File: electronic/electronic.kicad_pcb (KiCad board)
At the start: 2 copper layers, 19 parts, among them J1 M_BAT01, J10 BMP01, J11 MPU6050_01, J12 NEO_06_01, J14 OLED, J15 HCSR01, J16 HCSR01, J17 HCSR01, J18 HCSR01, J2 M_SIG01, J3 M_SIG01, J4 M_BAT01, J5 M_SIG01, J6 M_BAT01, J7 M_SIG01, J8 M_BAT01, J9 DHT01, U10 DEVKIT_V1_ESP32-WROOM-32

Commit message: chore: PCB design added to the project
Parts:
- added C17: 220u, Capacitor_THT:C_Radial_D8.0mm_H11.5mm_P3.50mm, F.Cu at (104.5, 52.5)
- added J19: BAT, custom:DG301-5.0-2P-1X, F.Cu at (98.0, 67.0)
- added U14: L7805, Package_TO_SOT_SMD:TO-252-2, F.Cu at (97.2, 50.5)
- J16: value HCSR01 -> HCSR02
- J17: value HCSR01 -> HCSR03
- J18: value HCSR01 -> HCSR04
- J3: value M_SIG01 -> M_SIG02
- J4: value M_BAT01 -> M_BAT02
- J5: value M_SIG01 -> M_SIG03
- J6: value M_BAT01 -> M_BAT03
- J7: value M_SIG01 -> M_SIG04
- J8: value M_BAT01 -> M_BAT04
- J9: footprint Connector_PinHeader_2.54mm:PinHeader_1x04_P2.54mm_Vertical -> custom:DHT22
- moved J16 125.8 mm to (17.5, 39.9)
- moved J6 113.0 mm to (21.0, 68.5), turned to 180 degrees
- moved J5 102.7 mm to (21.0, 61.5), turned to 180 degrees
- moved J12 90.7 mm to (64.9, 58.5), turned to 90 degrees
- moved J15 90.2 mm to (69.5, 18.0), turned to -90 degrees
- moved J2 88.4 mm to (18.5, 25.5)
- moved J14 81.7 mm to (94.9, 32.0), turned to 90 degrees
- moved J11 81.5 mm to (60.0, 30.8)
- moved J17 79.5 mm to (61.9, 68.5), turned to 90 degrees
- moved J1 78.3 mm to (21.0, 19.5), turned to 180 degrees
- moved R1 64.7 mm to (76.0, 43.7)
- moved J10 60.1 mm to (88.3, 25.0), turned to 90 degrees
- moved U10 54.0 mm to (39.8, 46.1)
- moved J4 51.3 mm to (112.5, 19.5), turned to 180 degrees
- moved J18 48.9 mm to (113.5, 46.5), turned to 180 degrees
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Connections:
- U10 pad 11: MOTOR04 -> MOTOR01
- U10 pad 12: MOTOR03 -> MOTOR02
- U10 pad 13: MOTOR02 -> MOTOR04
- U10 pad 15: MOTOR01 -> MOTOR03
- U10 pad 32: unconnected-(U10-GND2-Pad32) -> Earth
- U10 pad 38: unconnected-(U10-GND3-Pad38) -> Earth
- U10 pad 7: ULTRAE02 -> ULTRAT02
- U10 pad 8: ULTRAT02 -> ULTRAE02
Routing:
- net Earth: track 0.00 -> 338.3 mm, vias 0 -> 10
- net -BATT: track 0.00 -> 327.1 mm
- net +5V: track 0.00 -> 295.5 mm, vias 0 -> 11
- net +BATT: track 0.00 -> 237.9 mm, vias 0 -> 3
- net MOTOR04: track 0.00 -> 141.1 mm
- net MOTOR02: track 0.00 -> 114.8 mm
- net +3.3V: track 0.00 -> 86.4 mm, vias 0 -> 4
- net ULTRAE04: track 0.00 -> 78.5 mm
- net ULTRAT04: track 0.00 -> 78.2 mm
- net DHT_SIG: track 0.00 -> 70.5 mm, vias 0 -> 4
- net BMP_SCK01: track 0.00 -> 70.0 mm
- net BMP_SDI01: track 0.00 -> 69.9 mm
- net ULTRAT01: track 0.00 -> 67.5 mm
- net ULTRAE01: track 0.00 -> 60.6 mm
- net MOTOR01: track 0.00 -> 26.7 mm, vias 0 -> 2
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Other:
- board outline added: 105 x 62 mm

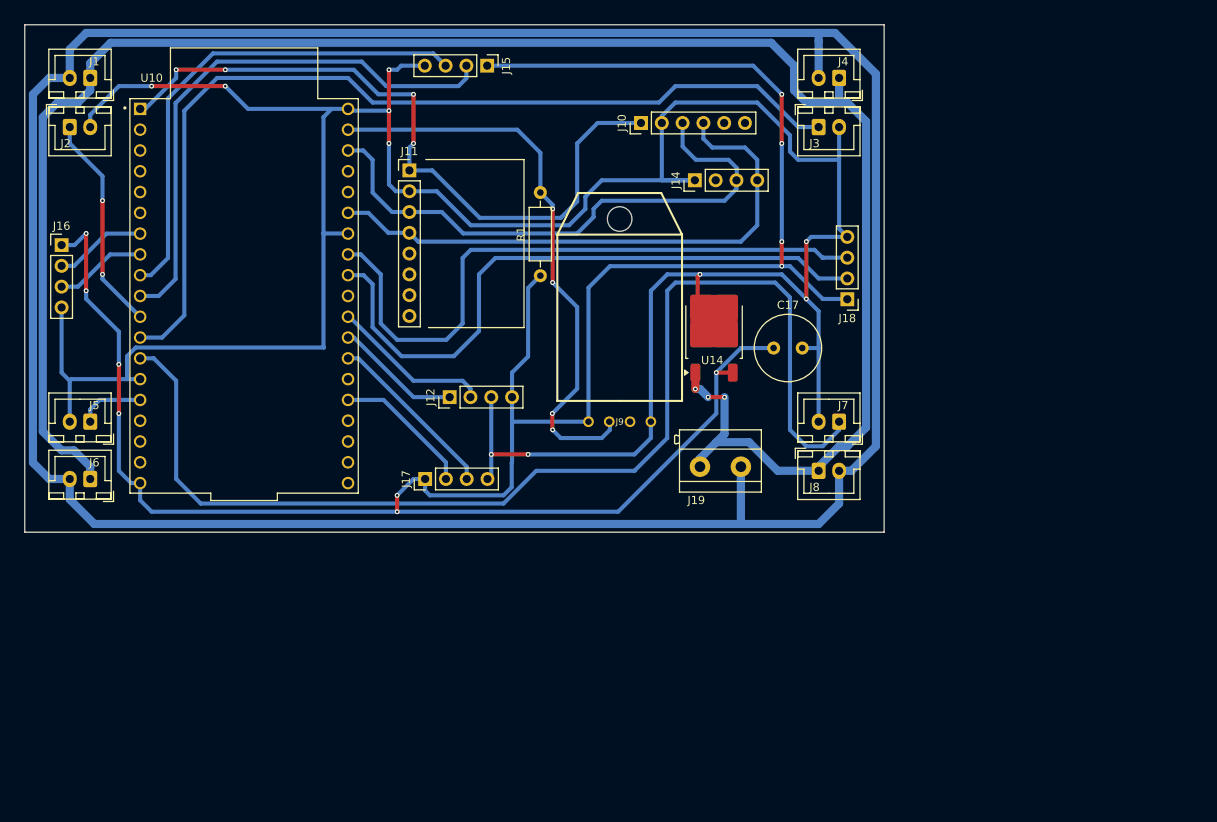
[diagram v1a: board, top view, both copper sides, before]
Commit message: refactor (electronic): update PCB design
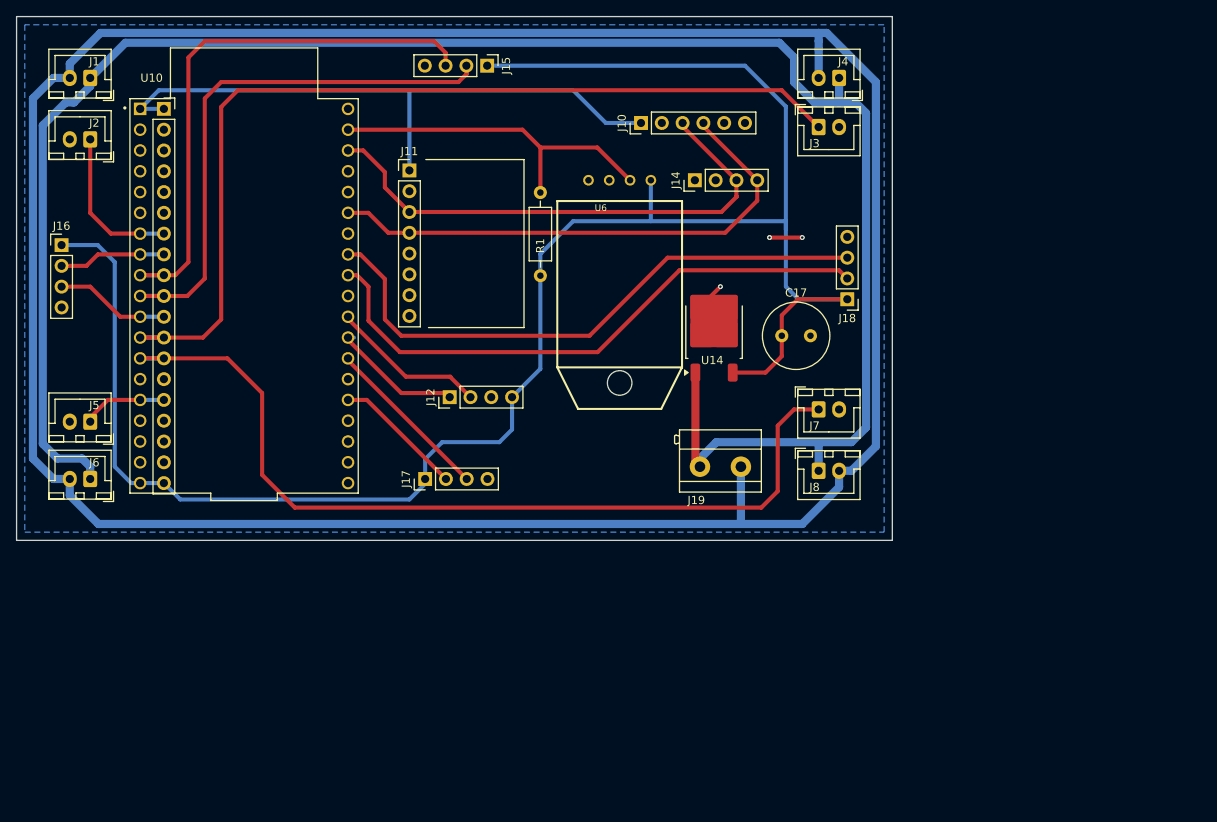
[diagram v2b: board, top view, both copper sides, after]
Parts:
- removed J9: DHT01, custom:DHT22
- added J20: 25.5-24 ESP32, Connector_PinSocket_2.54mm:PinSocket_1x19_P2.54mm_Vertical, F.Cu at (30.0, 23.3)
- added U6: DHT22, custom:DHT22, F.Cu at (85.7, 32.0)
- moved J2 2.92 mm to (21.0, 27.0), turned to 180 degrees
- moved J7 2.92 mm to (110.0, 60.0), turned to 0 degrees
- moved C17 1.80 mm to (105.5, 51.0)
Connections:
- U10 pad 11: MOTOR01 -> ULTRAE02
- U10 pad 7: ULTRAT02 -> MOTOR01
- U10 pad 8: ULTRAE02 -> ULTRAT02
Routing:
- net Earth: track 338.3 -> 8.47 mm, vias 10 -> 3
- net +5V: track 295.5 -> 237.8 mm, vias 11 -> 0
- net MOTOR04: track 141.1 -> 108.9 mm
- net DHT_SIG: track 70.5 -> 42.5 mm, vias 4 -> 0
- net +3.3V: track 86.4 -> 76.5 mm, vias 4 -> 0
- net ULTRAE01: track 60.6 -> 68.9 mm
- net MOTOR01: track 26.7 -> 19.0 mm, vias 2 -> 0
- net ULTRAE04: track 78.5 -> 72.0 mm
- net ULTRAT04: track 78.2 -> 71.9 mm
- net BMP_SCK01: track 70.0 -> 64.3 mm
- net BMP_SDI01: track 69.9 -> 64.9 mm
- net -BATT: track 327.1 -> 323.4 mm
- net ULTRAE02: track 11.2 -> 14.0 mm
- net MOTOR03: track 8.08 -> 10.4 mm
- net ULTRAT02: track 11.2 -> 13.1 mm
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- added copper zone on B.Cu, net Earth
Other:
- board size 105 x 62 mm -> 107 x 64 mm

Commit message: refactor (electronic, power): separate the project PCB in two
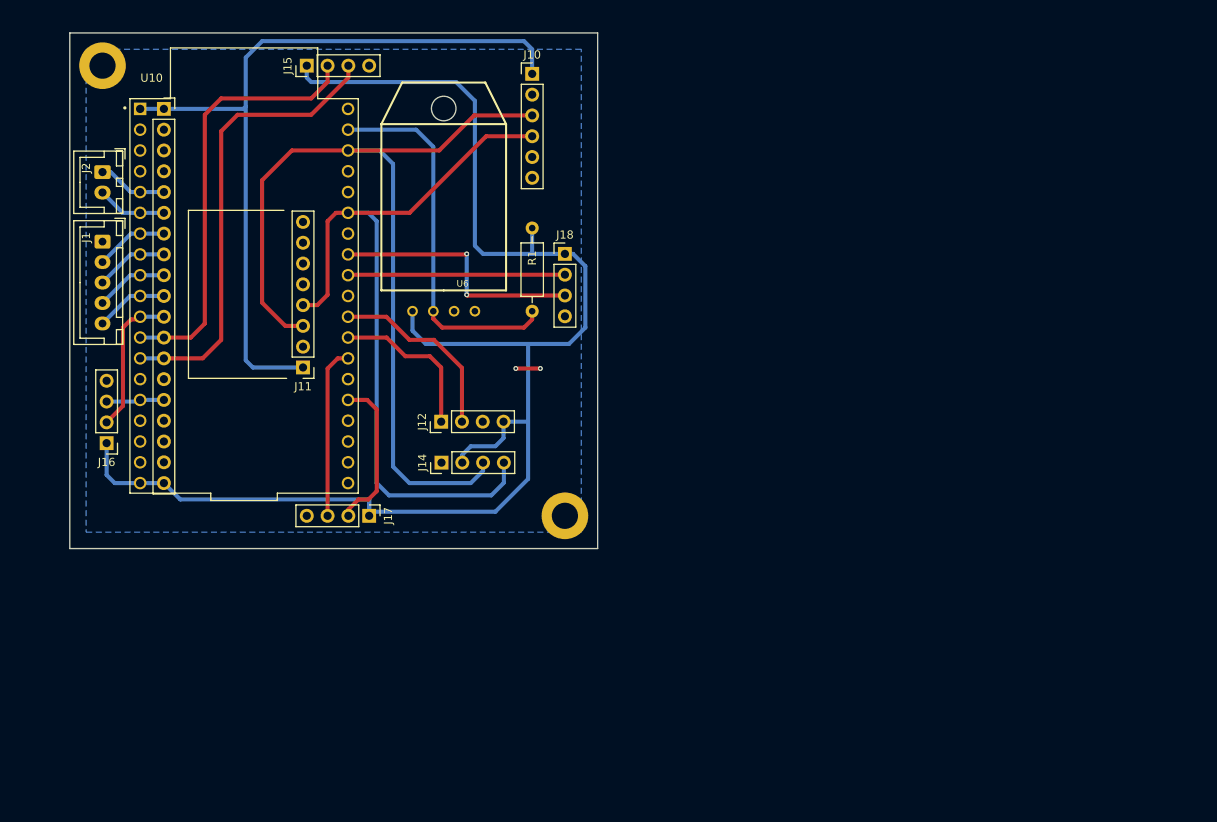
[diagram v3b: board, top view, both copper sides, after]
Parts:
- removed C17: 220u, Capacitor_THT:C_Radial_D8.0mm_H11.5mm_P3.50mm
- removed J19: BAT, custom:DG301-5.0-2P-1X
- removed J3: M_SIG02, Connector_JST:JST_XH_B2B-XH-A_1x02_P2.50mm_Vertical
- removed J4: M_BAT02, Connector_JST:JST_XH_B2B-XH-A_1x02_P2.50mm_Vertical
- removed J5: M_SIG03, Connector_JST:JST_XH_B2B-XH-A_1x02_P2.50mm_Vertical
- removed J6: M_BAT03, Connector_JST:JST_XH_B2B-XH-A_1x02_P2.50mm_Vertical
- removed J7: M_SIG04, Connector_JST:JST_XH_B2B-XH-A_1x02_P2.50mm_Vertical
- removed J8: M_BAT04, Connector_JST:JST_XH_B2B-XH-A_1x02_P2.50mm_Vertical
- removed U14: L7805, Package_TO_SOT_SMD:TO-252-2
- added REF**: MountingHole_3.2mm_M3_ISO7380_Pad, MountingHole:MountingHole_3.2mm_M3_ISO7380_Pad, F.Cu at (22.5, 18.0)
- added REF**: MountingHole_3.2mm_M3_ISO7380_Pad, MountingHole:MountingHole_3.2mm_M3_ISO7380_Pad, F.Cu at (79.0, 73.0)
- J1: value M_BAT01 -> M_PWM; footprint Connector_JST:JST_XH_B2B-XH-A_1x02_P2.50mm_Vertical -> Connector_JST:JST_XH_B5B-XH-A_1x05_P2.50mm_Vertical
- J2: value M_SIG01 -> BAT_AX
- moved J14 46.4 mm to (63.9, 66.5)
- moved J18 34.9 mm to (79.0, 41.0), turned to 0 degrees
- moved J11 27.4 mm to (47.0, 54.9), turned to 180 degrees
- moved U6 26.8 mm to (64.2, 48.0), turned to 0 degrees
- moved J16 24.8 mm to (23.0, 64.1), turned to 180 degrees
- moved J15 22.0 mm to (47.5, 18.0), turned to 90 degrees
- moved J1 20.1 mm to (22.5, 39.5), turned to -90 degrees
- moved J10 14.6 mm to (75.0, 19.0), turned to 0 degrees
- moved J17 8.19 mm to (55.1, 73.0), turned to -90 degrees
- moved R1 5.91 mm to (75.0, 37.8), turned to -90 degrees
- moved J2 4.27 mm to (22.5, 31.0), turned to -90 degrees
- moved J12 3.18 mm to (63.9, 61.5)
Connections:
- J1 pad 1: +BATT -> Earth
- J1 pad 2: -BATT -> MOTOR01
- J14 pad 2: +3V3 -> +5V
- J2 pad 1: MOTOR01 -> A01
- J2 pad 2: Earth -> A02
- J20 pad 10: ULTRAT01 -> MOTOR04
- J20 pad 11: ULTRAE02 -> ULTRAT02
- J20 pad 12: MOTOR02 -> ULTRAT01
- J20 pad 13: MOTOR04 -> ULTRAE01
- J20 pad 15: MOTOR03 -> ULTRAE02
- J20 pad 5: unconnected-(J20-Pin_5-Pad5) -> A01
- J20 pad 6: unconnected-(J20-Pin_6-Pad6) -> A02
- J20 pad 8: ULTRAT02 -> MOTOR02
- J20 pad 9: ULTRAE01 -> MOTOR03
- U10 pad 10: ULTRAT01 -> MOTOR04
- U10 pad 11: ULTRAE02 -> ULTRAT02
- U10 pad 12: MOTOR02 -> ULTRAT01
- U10 pad 13: MOTOR04 -> ULTRAE01
- U10 pad 15: MOTOR03 -> ULTRAE02
- U10 pad 5: unconnected-(U10-IO34-Pad5) -> A01
- U10 pad 6: unconnected-(U10-IO35-Pad6) -> A02
- U10 pad 8: ULTRAT02 -> MOTOR02
- U10 pad 9: ULTRAE01 -> MOTOR03
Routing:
- net -BATT: track 323.4 -> 0.00 mm
- net +BATT: track 237.6 -> 0.00 mm
- net MOTOR02: track 115.4 -> 8.92 mm
- net MOTOR04: track 108.9 -> 8.89 mm
- net +5V: track 237.8 -> 181.2 mm
- net BMP_SCK01: track 64.3 -> 114.0 mm
- net ULTRAT04: track 71.9 -> 26.5 mm
- net ULTRAE04: track 72.0 -> 31.6 mm, vias 0 -> 2
- net BMP_SDI01: track 64.9 -> 97.0 mm
- net +3.3V: track 76.5 -> 96.6 mm
- net ULTRAT01: track 67.9 -> 52.8 mm
- net ULTRAE01: track 68.9 -> 56.0 mm
- net MOTOR01: track 19.0 -> 8.94 mm
- net A02: track 0.00 -> 8.53 mm
- net A01: track 0.00 -> 8.51 mm
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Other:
- board size 107 x 64 mm -> 64.5 x 63 mm

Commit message: chore (electronic | power): update electronic subprojects
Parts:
- moved J1 4.01 mm to (18.5, 39.8)
- moved J10 4.01 mm to (71.0, 19.3)
- moved J11 4.01 mm to (43.0, 55.2)
- moved J12 4.01 mm to (59.9, 61.8)
- moved J15 4.01 mm to (43.5, 18.3)
- moved J18 4.01 mm to (75.0, 41.3)
- moved J2 4.01 mm to (18.5, 31.3)
- moved J20 4.01 mm to (26.0, 23.6)
- moved REF** 4.01 mm to (18.5, 18.3)
- moved U10 4.01 mm to (35.8, 46.5)
- moved U6 4.01 mm to (60.2, 48.3)
- moved J14 4.01 mm to (59.9, 66.8)
- moved J16 4.01 mm to (19.0, 64.4)
- moved J17 4.01 mm to (51.1, 73.3)
- moved R1 4.01 mm to (71.0, 38.2)
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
